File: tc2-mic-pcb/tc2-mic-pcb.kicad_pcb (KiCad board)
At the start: 2 copper layers, 39 x 12 mm, 14 parts, among them J401 Conn_02x03_Odd_Even, J402 Screw_Terminal_01x01, J403 Screw_Terminal_01x01, U401 AP7335-18SNG-7, U402 TXS0102DCT

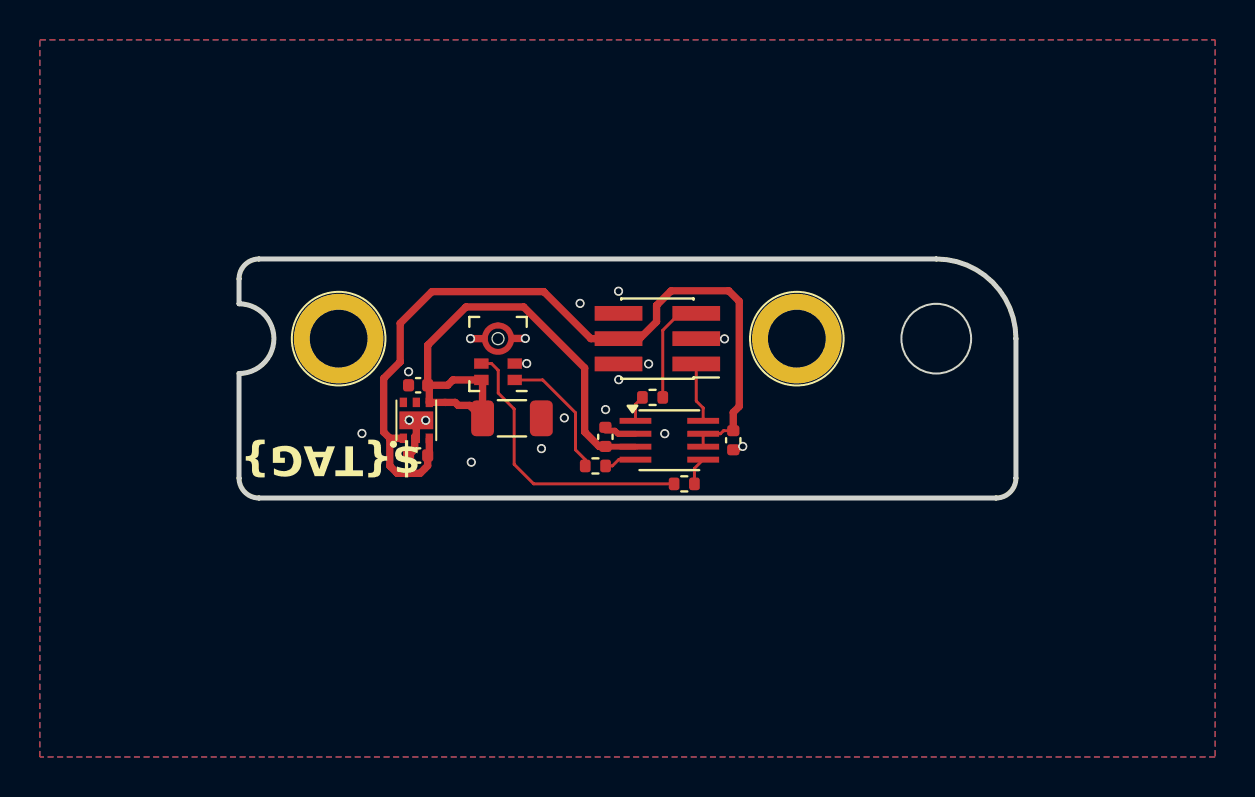
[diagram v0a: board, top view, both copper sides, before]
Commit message: Added pannel for microphone pcb
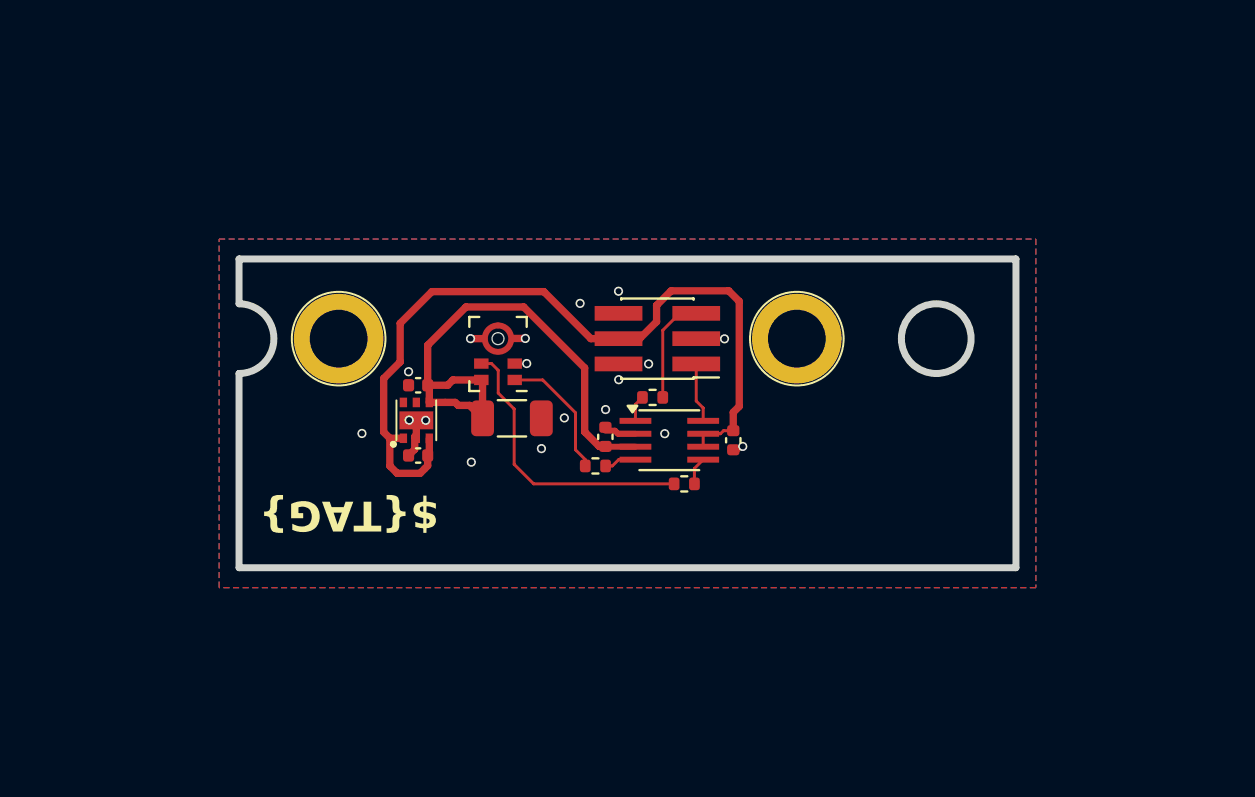
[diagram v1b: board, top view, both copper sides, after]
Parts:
- added REF**: Tab, PCM_kikit:Tab, F.Cu at (-6.00, 7.00)
- added REF**: Tab, PCM_kikit:Tab, F.Cu at (35.2, 7.00)
- added REF**: Tab, PCM_kikit:Tab, F.Cu at (14.0, 11.6)
- added REF**: Tab, PCM_kikit:Tab, F.Cu at (14.0, -4.55)
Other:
- board size 39 x 12 mm -> 39 x 15.5 mm

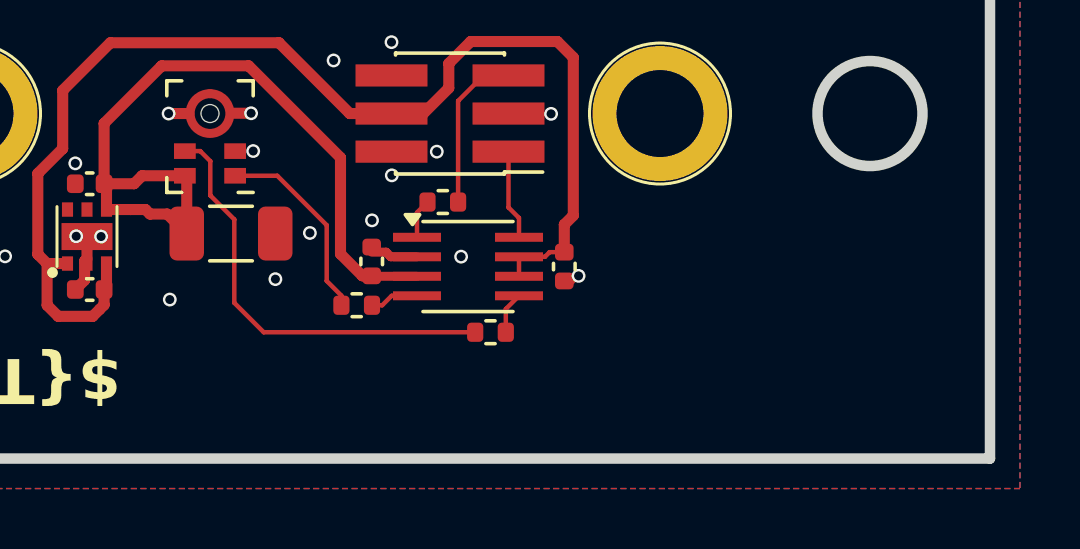
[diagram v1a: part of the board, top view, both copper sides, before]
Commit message: Add 2D barcode for microphone
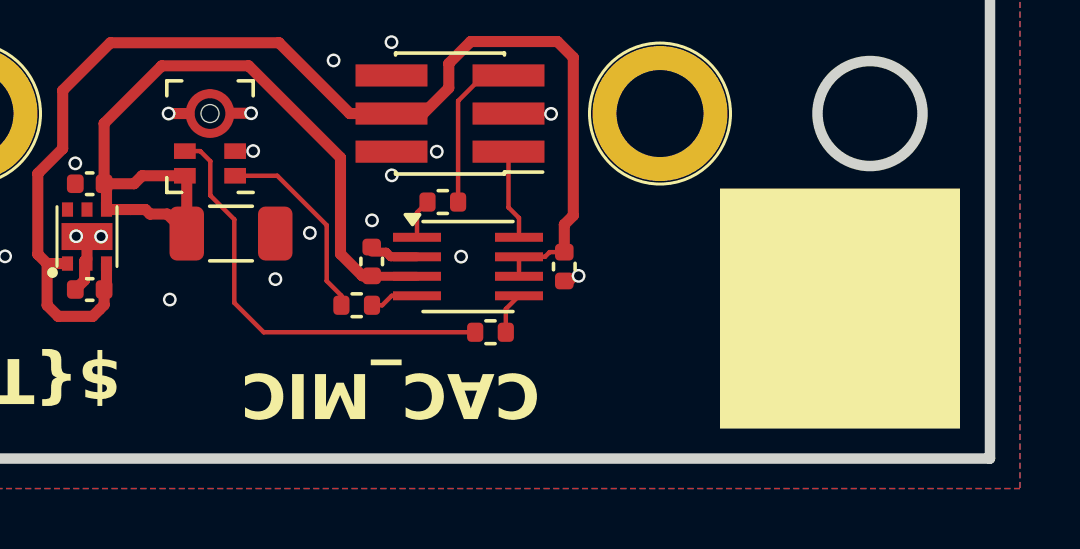
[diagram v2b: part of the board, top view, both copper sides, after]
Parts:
- added U403: ~, cacophony-library:JLCPCB_QR_8mm, F.Cu at (29.0, 6.50)
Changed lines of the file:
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@@
 			)
 		)
-		(property "KiLib_Generator" "connector/pin_header_socket"
-			(at 0 0 180)
-			(layer "F.SilkS")
-			(hide yes)
-			(effects
-				(font
-					(size 1 1)
-					(thickness 0.15)
-				)
-			)
-		)
 		(property "LCSC Part" "C5160759"
 			(at 0 0 0)
@@
 		(sheetname "/")
 		(sheetfile "tc2-mic-pcb.kicad_sch")
+		(units
+			(unit
+				(name "A")
+				(pins "1" "3" "5" "2" "4" "6")
+			)
+		)
 		(attr smd)
 		(duplicate_pad_numbers_are_jumpers no)
@@
 		(sheetname "/")
 		(sheetfile "tc2-mic-pcb.kicad_sch")
+		(units
+			(unit
+				(name "A")
+				(pins "1")
+			)
+		)
 		(attr smd)
 		(duplicate_pad_numbers_are_jumpers no)
@@
 		(sheetname "/")
 		(sheetfile "tc2-mic-pcb.kicad_sch")
+		(units
+			(unit
+				(name "A")
+				(pins "6" "5" "4" "3" "2" "7" "8" "1")
+			)
+		)
 		(attr smd)
 		(duplicate_pad_numbers_are_jumpers no)
@@
 		)
 	)
+	(footprint "cacophony-library:JLCPCB_QR_8mm"
+		(layer "F.Cu")
+		(at 29 6.5)
+		(property "Reference" "U403"
+			(at 0 -0.5 0)
+			(unlocked yes)
+			(layer "F.SilkS")
+			(hide yes)
+			(effects
+				(font
+					(size 1 1)
+					(thickness 0.1)
+				)
+			)
+		)
+		(property "Value" "~"
+			(at 0 1 0)
+			(unlocked yes)
+			(layer "F.Fab")
+			(effects
+				(font
+					(size 1 1)
+					(thickness 0.15)
+				)
+			)
+		)
+		(property "Datasheet" ""
+			(at 0 0 0)
+			(unlocked yes)
+			(layer "F.Fab")
+			(hide yes)
+			(effects
+				(font
+					(size 1 1)
+					(thickness 0.15)
+				)
+			)
+		)
+		(property "Description" ""
+			(at 0 0 0)
+			(unlocked yes)
+			(layer "F.Fab")
+			(hide yes)
+			(effects
+				(font
+					(size 1 1)
+					(thickness 0.15)
+				)
+			)
+		)
+		(sheetname "/")
+		(sheetfile "tc2-mic-pcb.kicad_sch")
+		(units
+			(unit
+				(name "A")
+				(pins)
+			)
+		)
+		(attr exclude_from_pos_files exclude_from_bom)
+		(duplicate_pad_numbers_are_jumpers no)
+		(fp_rect
+			(start -4 -4)
+			(end 4 4)
+			(stroke
+				(width 0)
+				(type solid)
+			)
+			(fill yes)
+			(layer "F.SilkS")
+		)
+		(fp_rect
+			(start -4 -4)
+			(end 4 4)
+			(stroke
+				(width 0.05)
+				(type default)
+			)
+			(fill no)
+			(layer "F.CrtYd")
+		)
+		(fp_text user "${REFERENCE}"
+			(at 0 2.5 0)
+			(unlocked yes)
+			(layer "F.Fab")
+			(effects
+				(font
+					(size 1 1)
+					(thickness 0.15)
+				)
+			)
+		)
+		(embedded_fonts no)
+	)
 	(footprint "PCM_kikit:Tab"
 		(layer "F.Cu")
@@
 		(sheetname "/")
 		(sheetfile "tc2-mic-pcb.kicad_sch")
+		(units
+			(unit
+				(name "A")
+				(pins "3" "1" "2" "4" "6" "5" "7")
+			)
+		)
 		(attr smd)
 		(duplicate_pad_numbers_are_jumpers no)
@@
 			)
 		)
-		(property "KiLib_Generator" "C1525"
-			(at 0 0 0)
+		(property "LCSC Part" "C1525"
+			(at 0 0 90)
+			(unlocked yes)
 			(layer "F.Fab")
 			(hide yes)
@@
 		(sheetname "/")
 		(sheetfile "tc2-mic-pcb.kicad_sch")
+		(units
+			(unit
+				(name "A")
+				(pins "1" "2")
+			)
+		)
 		(attr smd)
 		(duplicate_pad_numbers_are_jumpers no)
@@
 			)
 		)
-		(property "KiLib_Generator" "SMD_2terminal_chip_molded"
-			(at 0 0 0)
-			(layer "F.SilkS")
-			(hide yes)
-			(effects
-				(font
-					(size 1 1)
-					(thickness 0.15)
-				)
-			)
-		)
 		(property "LCSC Part" "C170182"
 			(at 0 0 0)
@@
 		(sheetname "/")
 		(sheetfile "tc2-mic-pcb.kicad_sch")
+		(units
+			(unit
+				(name "A")
+				(pins "1" "2")
+			)
+		)
 		(attr smd)
 		(duplicate_pad_numbers_are_jumpers no)
@@
 		(sheetname "/")
 		(sheetfile "tc2-mic-pcb.kicad_sch")
+		(units
+			(unit
+				(name "A")
+				(pins "1")
+			)
+		)
 		(attr smd)
 		(duplicate_pad_numbers_are_jumpers no)
@@
 			)
 		)
-		(property "KiLib_Generator" "C25092"
+		(property "LCSC Part" "C25092"
 			(at 0 0 0)
+			(unlocked yes)
 			(layer "F.Fab")
 			(hide yes)
@@
 		(sheetname "/")
 		(sheetfile "tc2-mic-pcb.kicad_sch")
+		(units
+			(unit
+				(name "A")
+				(pins "1" "2")
+			)
+		)
 		(attr smd)
 		(duplicate_pad_numbers_are_jumpers no)
@@
 			)
 		)
-		(property "KiLib_Generator" "C52923"
-			(at 0 0 0)
+		(property "LCSC Part" "C52923"
+			(at 0 0 180)
+			(unlocked yes)
 			(layer "F.Fab")
 			(hide yes)
@@
 		(sheetname "/")
 		(sheetfile "tc2-mic-pcb.kicad_sch")
+		(units
+			(unit
+				(name "A")
+				(pins "1" "2")
+			)
+		)
 		(attr smd)
 		(duplicate_pad_numbers_are_jumpers no)
@@
 			)
 		)
-		(property "KiLib_Generator" "C25092"
+		(property "LCSC Part" "C25092"
 			(at 0 0 0)
+			(unlocked yes)
 			(layer "F.Fab")
 			(hide yes)
@@
 		(sheetname "/")
 		(sheetfile "tc2-mic-pcb.kicad_sch")
+		(units
+			(unit
+				(name "A")
+				(pins "1" "2")
+			)
+		)
 		(attr smd)
 		(duplicate_pad_numbers_are_jumpers no)
@@
 			)
 		)
-		(property "KiLib_Generator" "C1525"
-			(at 0 0 0)
+		(property "LCSC Part" "C1525"
+			(at 0 0 270)
+			(unlocked yes)
 			(layer "F.Fab")
 			(hide yes)
@@
 		(sheetname "/")
 		(sheetfile "tc2-mic-pcb.kicad_sch")
+		(units
+			(unit
+				(name "A")
+				(pins "1" "2")
+			)
+		)
 		(attr smd)
 		(duplicate_pad_numbers_are_jumpers no)
@@
 			)
 		)
-		(property "KiLib_Generator" "C25092"
+		(property "LCSC Part" "C25092"
 			(at 0 0 0)
+			(unlocked yes)
 			(layer "F.Fab")
 			(hide yes)
@@
 		(sheetname "/")
 		(sheetfile "tc2-mic-pcb.kicad_sch")
+		(units
+			(unit
+				(name "A")
+				(pins "1" "2")
+			)
+		)
 		(attr smd)
 		(duplicate_pad_numbers_are_jumpers no)
@@
 			)
 		)
-		(property "KiLib_Generator" "C52923"
-			(at 0 0 0)
+		(property "LCSC Part" "C52923"
+			(at 0 0 180)
+			(unlocked yes)
 			(layer "F.Fab")
 			(hide yes)
@@
 		(sheetname "/")
 		(sheetfile "tc2-mic-pcb.kicad_sch")
+		(units
+			(unit
+				(name "A")
+				(pins "1" "2")
+			)
+		)
 		(attr smd)
 		(duplicate_pad_numbers_are_jumpers no)
@@
 			)
 		)
-		(property "LCSC" "C2879853"
-			(at 0 0 0)
+		(property "LCSC Part" "C2879853"
+			(at 0 0 180)
+			(unlocked yes)
 			(layer "F.Fab")
 			(hide yes)
@@
 		(sheetname "/")
 		(sheetfile "tc2-mic-pcb.kicad_sch")
+		(units
+			(unit
+				(name "A")
+				(pins "5" "3" "2" "4" "1")
+			)
+		)
 		(attr smd)
 		(duplicate_pad_numbers_are_jumpers no)
@@
 		(layer "User.7")
 	)
-	(gr_text "${TAG}"
-		(at -4 8 180)
+	(gr_text "CAC_MIC"
+		(at 19 8.5 180)
 		(layer "F.SilkS")
 		(effects
@@
 				(bold yes)
 			)
-			(justify right bottom)
+			(justify left bottom)
 		)
 	)
-	(gr_text "CAC_MIC"
-		(at 31.5 7.33 0)
-		(layer "B.SilkS")
+	(gr_text "${TAG}"
+		(at -4 8 180)
+		(layer "F.SilkS")
 		(effects
 			(font
@@
 				(bold yes)
 			)
-			(justify left bottom mirror)
+			(justify right bottom)
 		)
 	)

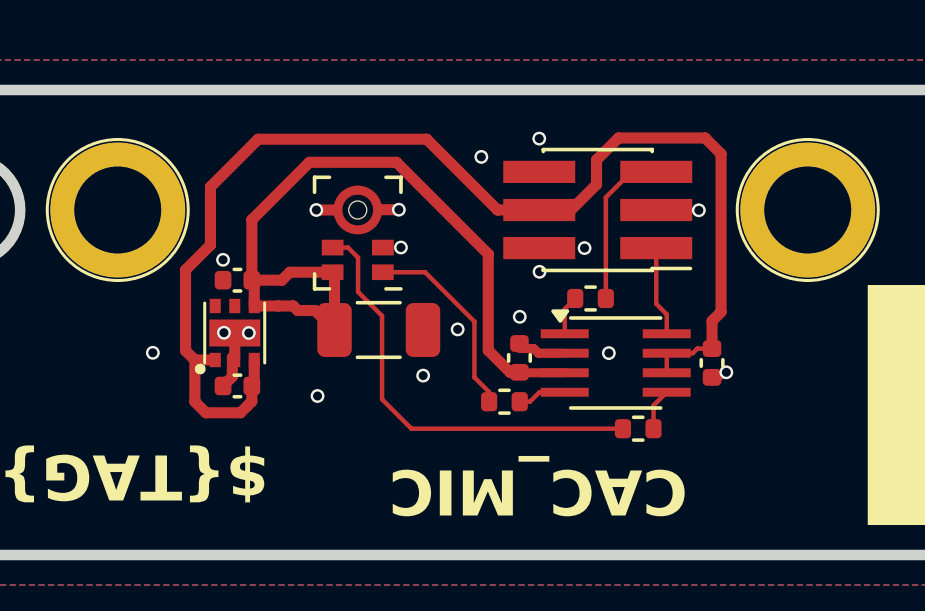
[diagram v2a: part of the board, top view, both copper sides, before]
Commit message: Add JLPCPCB 2D barcode to PCBs
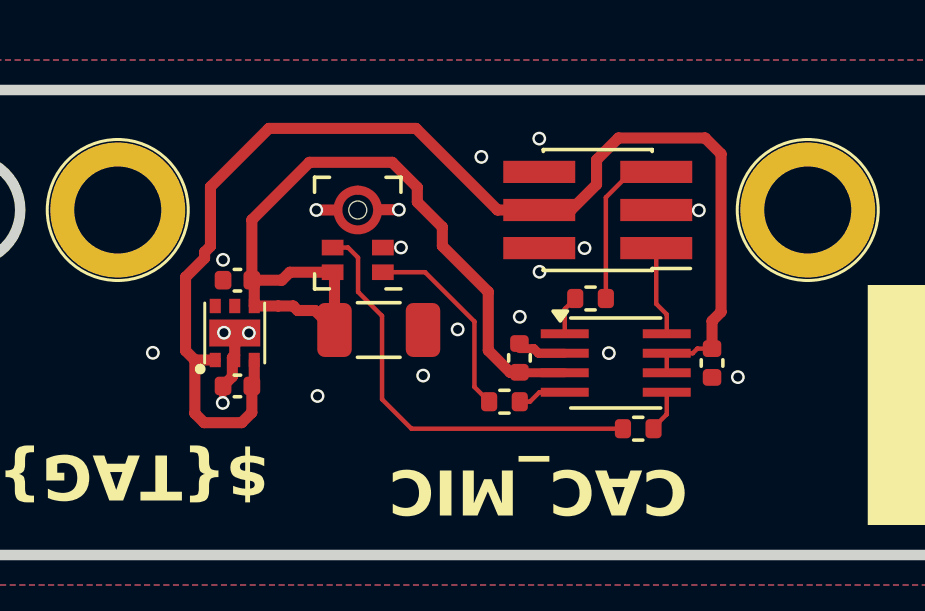
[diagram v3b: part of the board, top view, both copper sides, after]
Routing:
- net +3V3: track 41.0 -> 42.0 mm
- net GND: track 6.09 -> 6.04 mm, vias 18 -> 19

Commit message: Update tc2-micophone panelization
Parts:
- turned U403 to -90 degrees
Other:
- board text added: "${HASH}"
- board text removed: "CAC_MIC"
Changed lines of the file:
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@@
 	(footprint "cacophony-library:JLCPCB_QR_8mm"
 		(layer "F.Cu")
-		(at 29 6.5)
+		(at 29 6.5 -90)
 		(property "Reference" "U403"
-			(at 0 -0.5 0)
+			(at 0 -0.5 270)
 			(unlocked yes)
 			(layer "F.SilkS")
@@
 		)
 		(property "Value" "~"
-			(at 0 1 0)
+			(at 0 1 270)
 			(unlocked yes)
 			(layer "F.Fab")
@@
 		)
 		(property "Datasheet" ""
-			(at 0 0 0)
+			(at 0 0 270)
 			(unlocked yes)
 			(layer "F.Fab")
@@
 		)
 		(property "Description" ""
-			(at 0 0 0)
+			(at 0 0 270)
 			(unlocked yes)
 			(layer "F.Fab")
@@
 		)
 		(fp_text user "${REFERENCE}"
-			(at 0 2.5 0)
+			(at 0 2.5 270)
 			(unlocked yes)
 			(layer "F.Fab")
@@
 		(layer "User.7")
 	)
-	(gr_text "CAC_MIC"
-		(at 19 8.5 180)
+	(gr_text "${HASH}"
+		(at 18.47 8.49 -180)
 		(layer "F.SilkS")
 		(effects
